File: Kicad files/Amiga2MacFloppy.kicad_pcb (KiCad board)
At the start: 2 copper layers, 44 x 48 mm, 12 parts, among them J1 DB23F, J2 Conn_02x10_Odd_Even_MountingP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, J3 DB23M, U1 74LS139, U2 74LS393

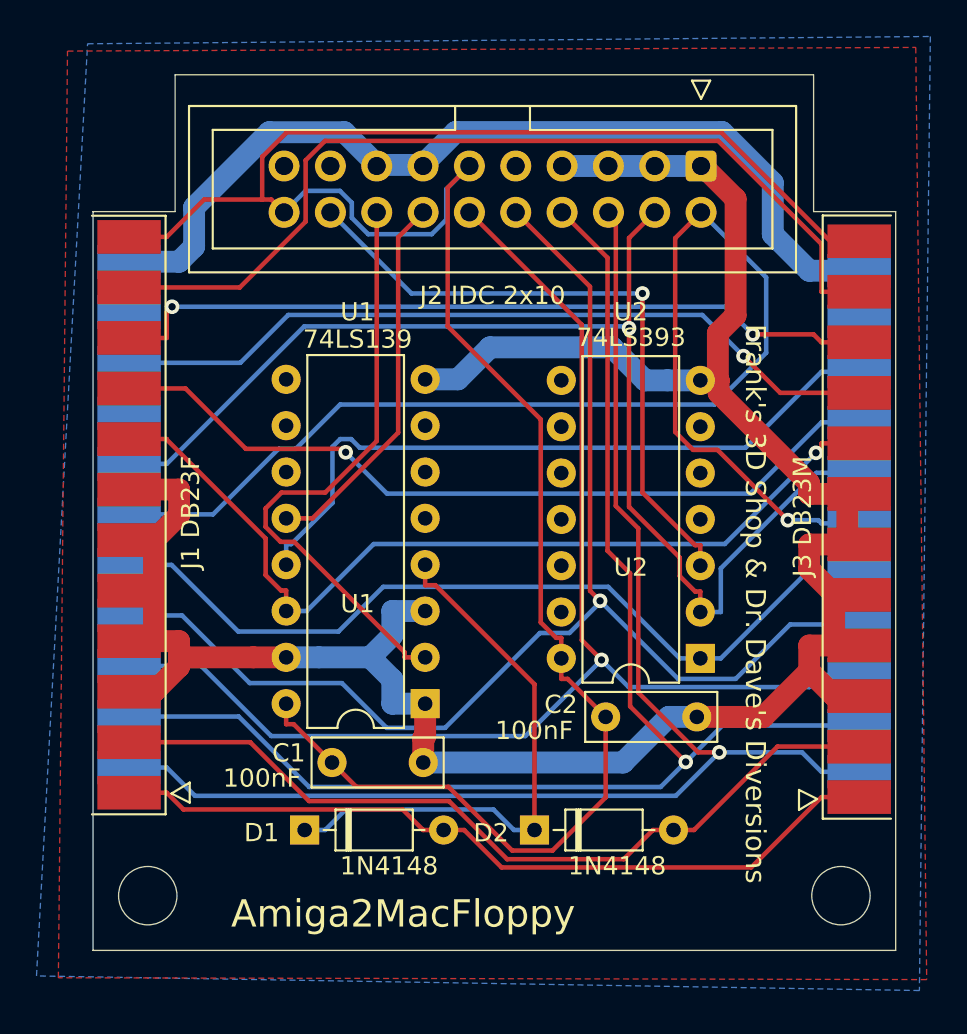
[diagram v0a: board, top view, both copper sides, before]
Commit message: Corrections
Corrected a missing trace pin 22 of both DB23.

Updated the Gerber files.
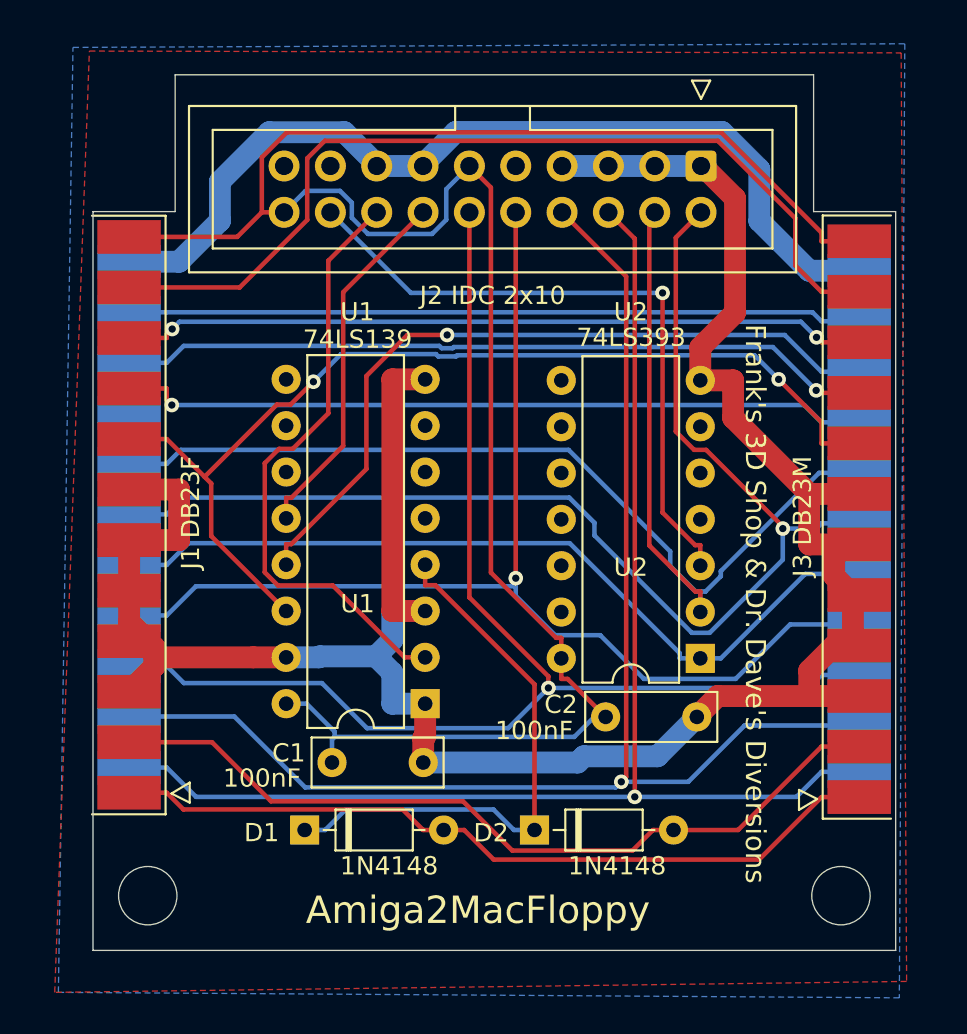
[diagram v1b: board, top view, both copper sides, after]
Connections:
- J1 pad 20: (no net) -> Net-(J1-Pad20)
- J1 pad 22: (no net) -> _INDEX
- J2 pad 17: (no net) -> Net-(J2-Pad17)
- J2 pad 19: (no net) -> Net-(J2-Pad19)
- J2 pad 9: (no net) -> Net-(J2-Pad9)
- J3 pad 22: (no net) -> _INDEX
- U1 pad 10: (no net) -> Net-(U1-Pad10)
- U1 pad 11: (no net) -> Net-(U1-Pad11)
- U1 pad 5: (no net) -> Net-(U1-Pad5)
- U1 pad 6: (no net) -> Net-(U1-Pad6)
- U1 pad 7: (no net) -> Net-(U1-Pad7)
- U1 pad 9: (no net) -> Net-(U1-Pad9)
- U2 pad 10: (no net) -> Net-(U2-Pad10)
- U2 pad 11: (no net) -> Net-(U2-Pad11)
- U2 pad 12: (no net) -> Net-(U2-Pad12)
- U2 pad 13: (no net) -> Net-(U2-Pad13)
- U2 pad 4: (no net) -> Net-(U2-Pad4)
- U2 pad 5: (no net) -> Net-(U2-Pad5)
- U2 pad 6: (no net) -> Net-(U2-Pad6)
- U2 pad 8: (no net) -> Net-(U2-Pad8)
- U2 pad 9: (no net) -> Net-(U2-Pad9)
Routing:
- net _INDEX: track 0.00 -> 40.2 mm
- net +5V: track 124.2 -> 116.8 mm
- net _DKWE: track 71.7 -> 64.8 mm
- net _MTRXD: track 49.7 -> 55.6 mm, vias 1 -> 2
- net PH0: track 72.6 -> 68.1 mm
- net GND: track 138.8 -> 135.3 mm
- net DIR: track 68.1 -> 71.4 mm, vias 1 -> 0
- net _SEL3: track 44.0 -> 41.2 mm
- net _SEL1: track 38.7 -> 41.1 mm, vias 0 -> 1
- net _DRES: track 42.4 -> 41.0 mm
- net _SEL2: track 42.9 -> 41.5 mm
- net SEL: track 71.8 -> 70.5 mm
- net PH2: track 74.9 -> 73.9 mm
- net _DKWD: track 46.1 -> 45.2 mm
- net _ENABLE: track 20.7 -> 20.0 mm
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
